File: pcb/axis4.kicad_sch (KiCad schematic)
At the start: 10 parts, among them J14 Mini v1.0 FEMALE sockets, J24 MOTOR PHASES male 1x3, J34 ENCODER JST-SH 6p, J44 MINI POWER: +12V / GND

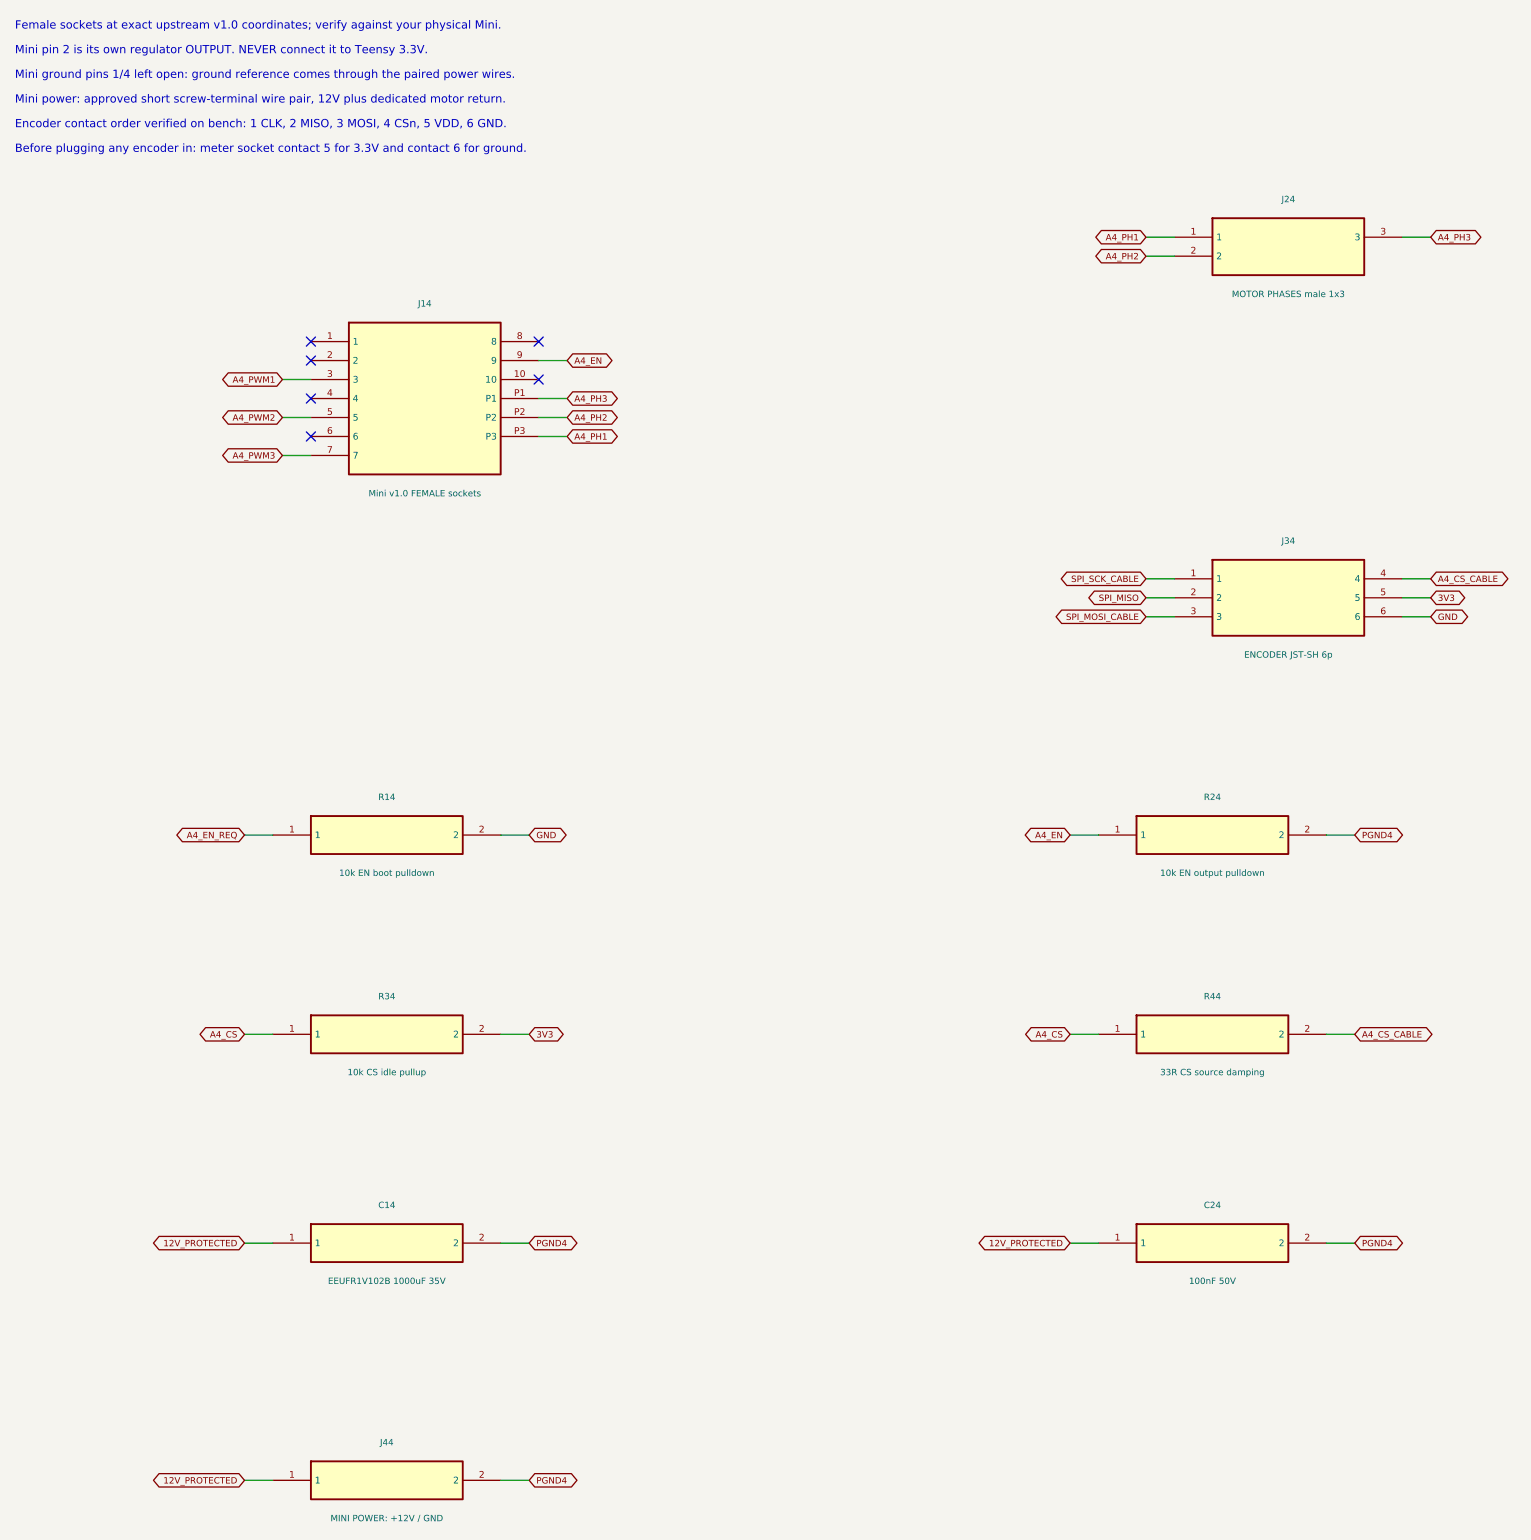
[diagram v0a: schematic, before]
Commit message: feat: finish through-hole six-axis carrier review design
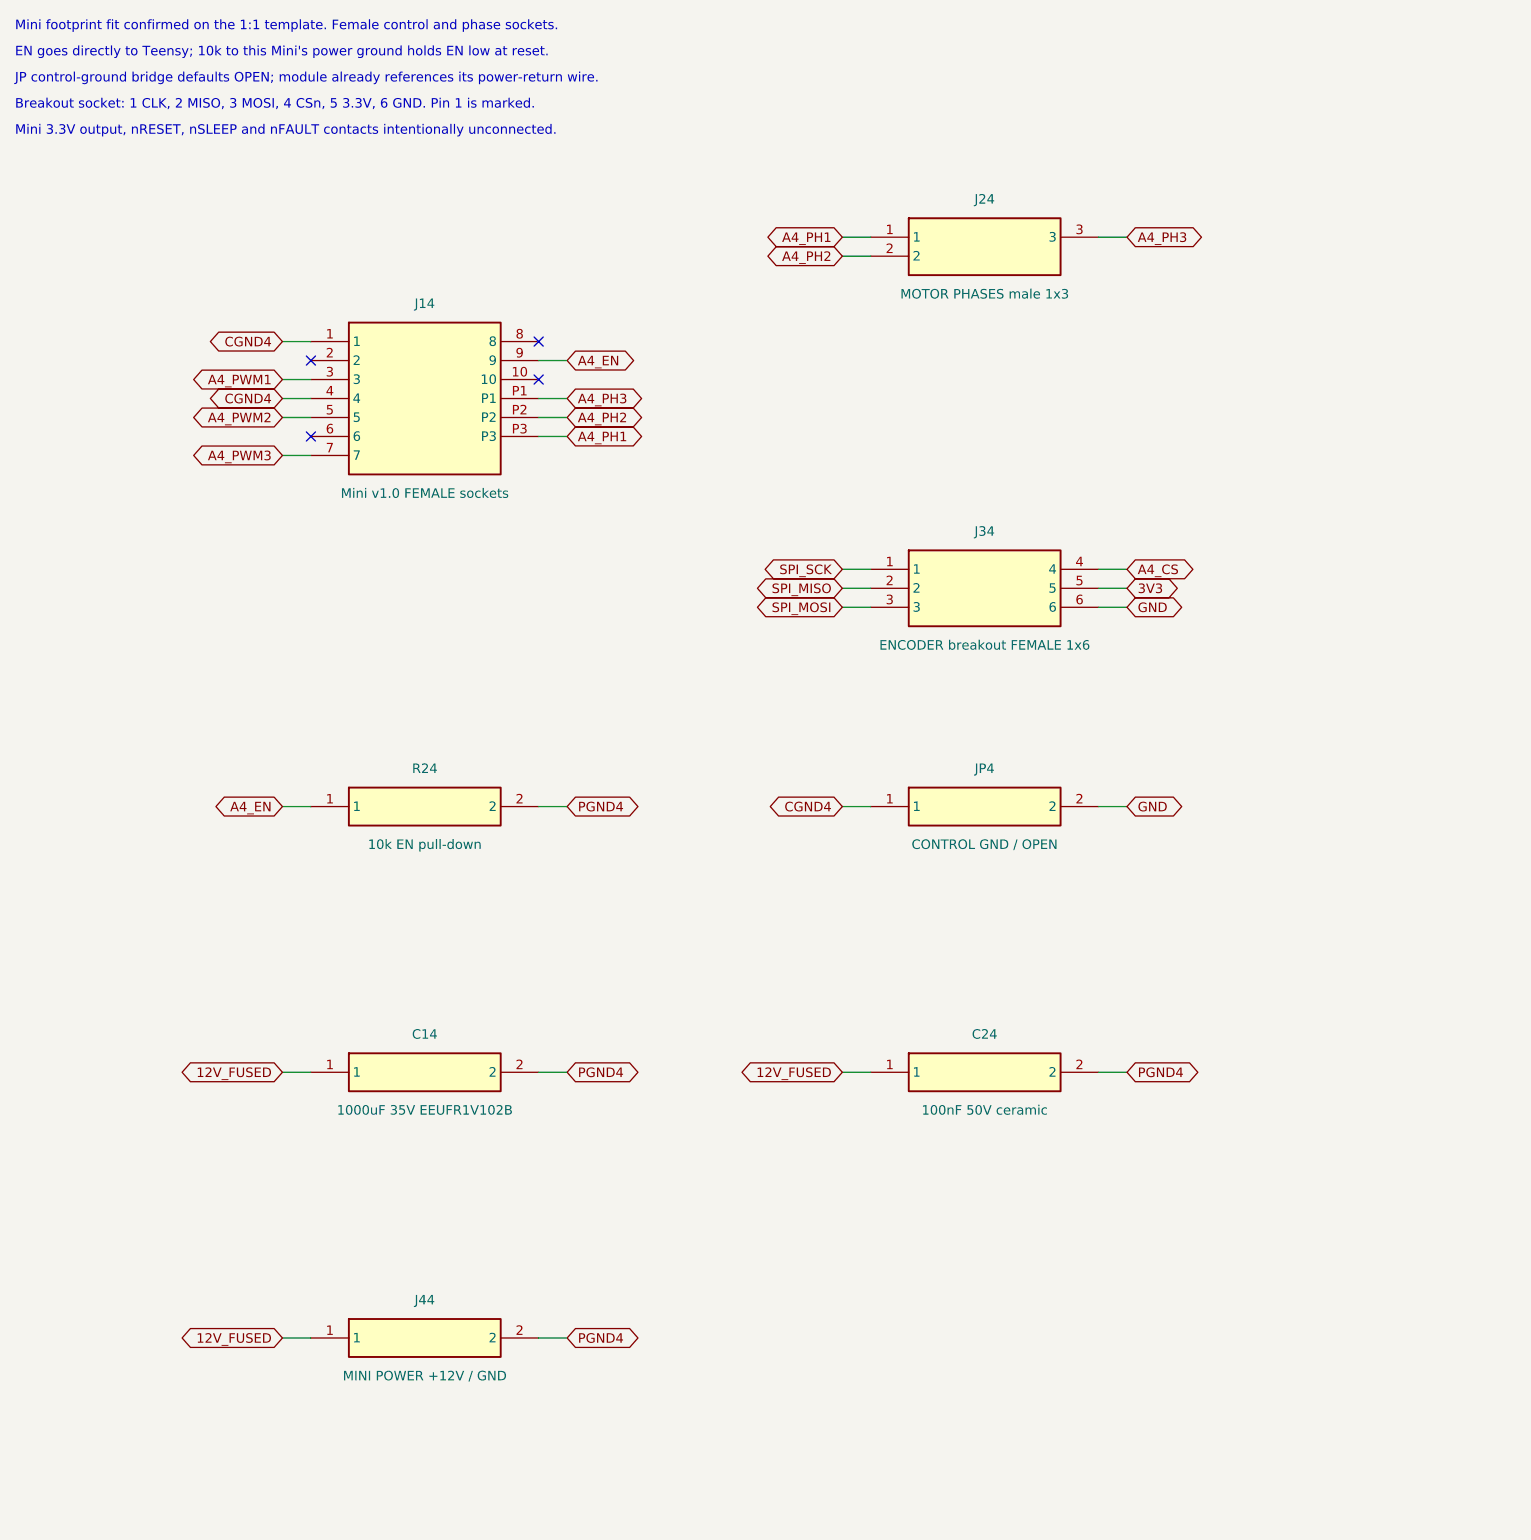
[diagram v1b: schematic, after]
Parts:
- removed R14: 10k EN boot pulldown, Resistor_SMD:R_0603_1608Metric, symbol TrueSkate:R14
- removed R34: 10k CS idle pullup, Resistor_SMD:R_0603_1608Metric, symbol TrueSkate:R34
- removed R44: 33R CS source damping, Resistor_SMD:R_0603_1608Metric, symbol TrueSkate:R44
- added JP4: CONTROL GND / OPEN, TrueSkate:GroundBridge_THT, symbol TrueSkate:JP4
- C14: value EEUFR1V102B 1000uF 35V -> 1000uF 35V EEUFR1V102B; LCSC C128476 -> (none)
- C24: value 100nF 50V -> 100nF 50V ceramic; footprint Capacitor_SMD:C_0603_1608Metric -> Capacitor_THT:C_Disc_D5.0mm_W2.5mm_P5.00mm; LCSC C14663 -> (none)
- J34: value ENCODER JST-SH 6p -> ENCODER breakout FEMALE 1x6; footprint Connector_JST:JST_SH_BM06B-SRSS-TB_1x06-1MP_P1.00mm_Vertical -> Connector_PinSocket_2.54mm:PinSocket_1x06_P2.54mm_Vertical; LCSC C160392 -> (none)
- J44: value MINI POWER: +12V / GND -> MINI POWER +12V / GND
- R24: value 10k EN output pulldown -> 10k EN pull-down; footprint Resistor_SMD:R_0603_1608Metric -> Resistor_THT:R_Axial_DIN0207_L6.3mm_D2.5mm_P7.62mm_Horizontal; LCSC C25804 -> (none)
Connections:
- net A4_CS_CABLE is gone; now on net A4_CS: J34.4
- net GND: now also JP4.2
- net CGND4: now reaches J14.1
- net CGND4: now also J14.4, JP4.1
- net 12V_PROTECTED renamed 12V_FUSED
- net SPI_MOSI_CABLE renamed SPI_MOSI
- net SPI_SCK_CABLE renamed SPI_SCK
- no-connect marks 6 -> 4
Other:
- note added: "Breakout socket: 1 CLK, 2 MISO, 3 MOSI, 4 CSn, 5 3.3V, 6 GND. Pin 1 is marked."
- note added: "EN goes directly to Teensy; 10k to this Mini's power ground holds EN low at reset."
- note added: "JP control-ground bridge defaults OPEN; module already references its power-return wire."
- note added: "Mini 3.3V output, nRESET, nSLEEP and nFAULT contacts intentionally unconnected."
- note added: "Mini footprint fit confirmed on the 1:1 template. Female control and phase sockets."
- note removed: "Before plugging any encoder in: meter socket contact 5 for 3.3V and contact 6 for ground."
- note removed: "Encoder contact order verified on bench: 1 CLK, 2 MISO, 3 MOSI, 4 CSn, 5 VDD, 6 GND."
- note removed: "Female sockets at exact upstream v1.0 coordinates; verify against your physical Mini."
- note removed: "Mini ground pins 1/4 left open: ground reference comes through the paired power wires."
- note removed: "Mini pin 2 is its own regulator OUTPUT. NEVER connect it to Teensy 3.3V."
- note removed: "Mini power: approved short screw-terminal wire pair, 12V plus dedicated motor return."
- title: 06 / Axis 4: middle_curl_1 -> 05 / A4: middle_curl_1
- moved on the sheet: C14, C24, J24, J34, J44, R24

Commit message: feat: use exact Mini v1.0 footprints with direct power routing
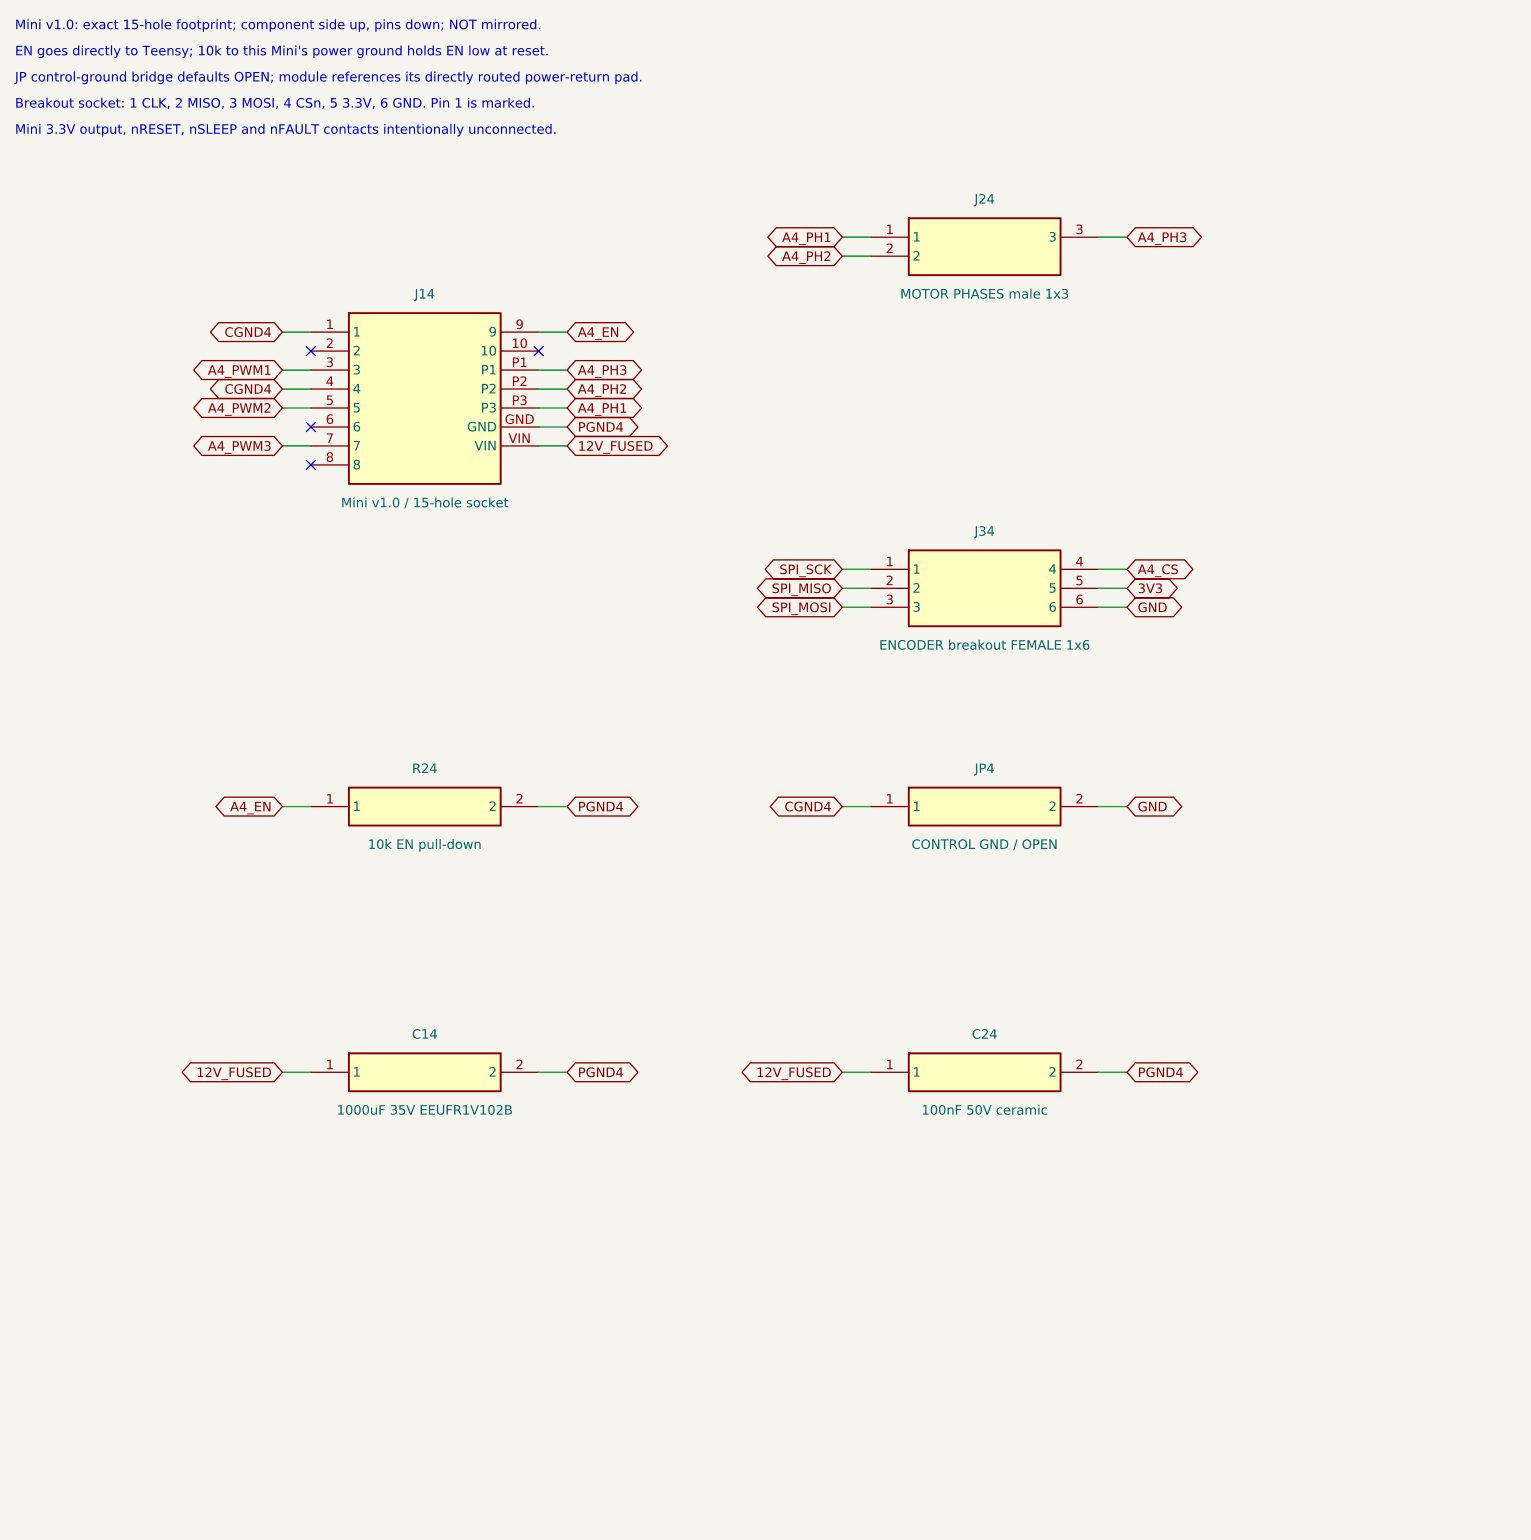
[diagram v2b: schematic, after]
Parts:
- removed J44: MINI POWER +12V / GND, TerminalBlock_Phoenix:TerminalBlock_Phoenix_MKDS-1-2-3.81_1x02_P3.81mm_Horizontal, symbol TrueSkate:J44
- J14: value Mini v1.0 FEMALE sockets -> Mini v1.0 / 15-hole socket; footprint TrueSkate:Mini_v1_Sockets -> TrueSkate:SimpleFOC_Mini_v1.0
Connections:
- net 12V_FUSED: now also J14.VIN
- net PGND4: now also J14.GND
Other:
- note added: "JP control-ground bridge defaults OPEN; module references its directly routed power-return pad."
- note added: "Mini v1.0: exact 15-hole footprint; component side up, pins down; NOT mirrored."
- note removed: "JP control-ground bridge defaults OPEN; module already references its power-return wire."
- note removed: "Mini footprint fit confirmed on the 1:1 template. Female control and phase sockets."
